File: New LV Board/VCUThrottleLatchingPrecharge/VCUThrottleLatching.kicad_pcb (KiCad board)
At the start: 2 copper layers, 70.3 x 45 mm, 30 parts, among them J1 B12B-PH-K-S:JST_B12B-PH-K-S, Q1 SS8550, U1 IRLML2060TRPBF, U2 IRLML2060TRPBF, U3 IRLML2060TRPBF, U5 IRLML2060TRPBF, U6 IRLML2060TRPBF, U8 PMV160UP, U9 NE555D

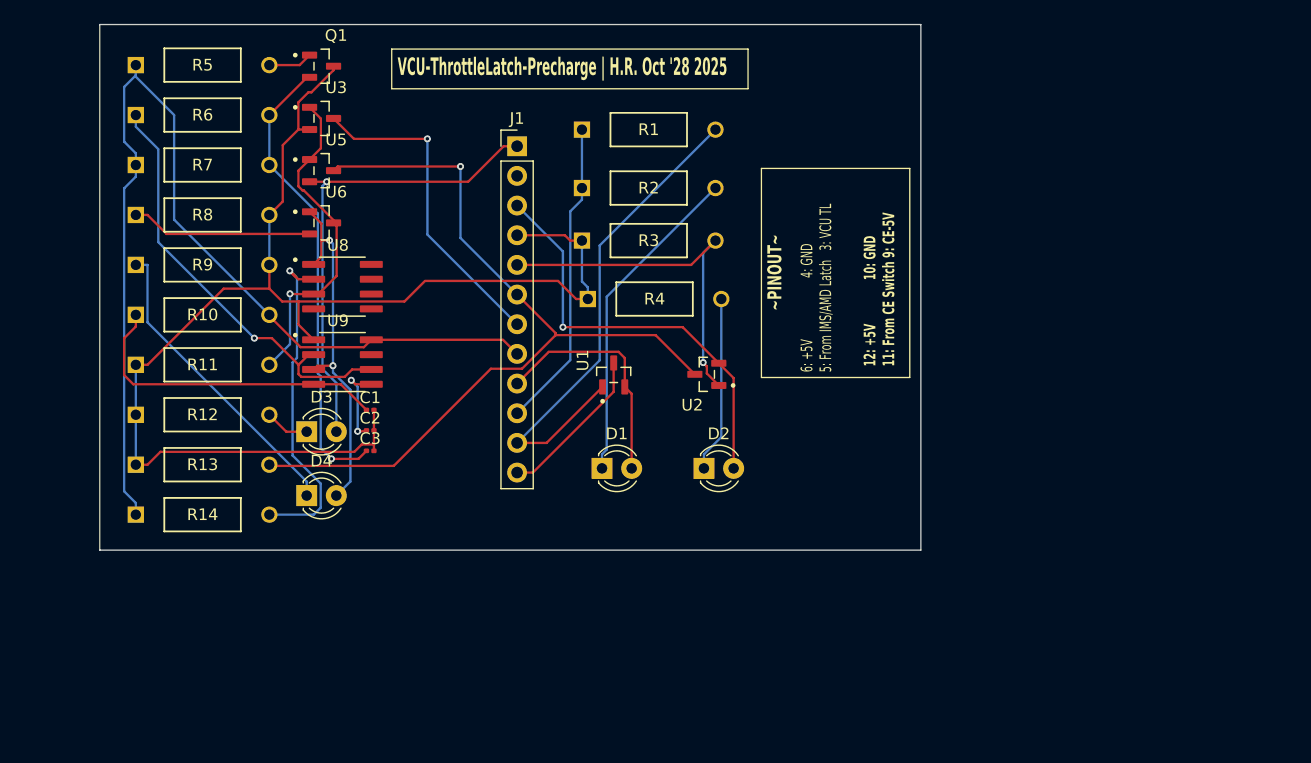
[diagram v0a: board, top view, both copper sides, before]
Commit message: Precharge module added along with file name change
Precharge module added along with file name change
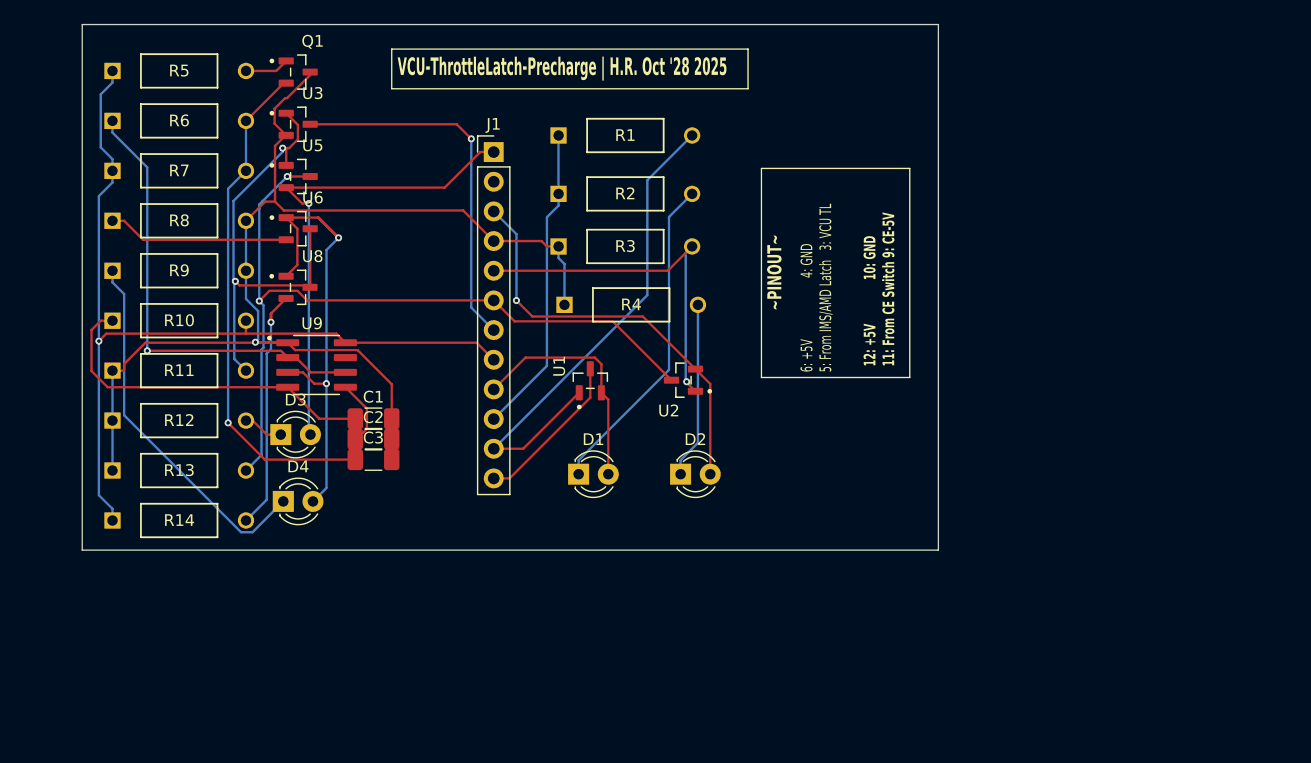
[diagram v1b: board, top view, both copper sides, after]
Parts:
- C1, C2, C3: footprint Capacitor_SMD:C_0201_0603Metric -> Capacitor_SMD:C_1206_3216Metric_Pad1.33x1.80mm_HandSolder
- U8: footprint Footprints:SOIC127P599X175-8N -> Footprints:SOT95P237X112-3N
- moved U8 3.81 mm to (99.5, 93.5)
- moved D3 2.23 mm to (98.0, 106.1)
- moved U9 2.23 mm to (101.1, 100.1)
- moved D1 2.06 mm to (123.5, 109.5)
- moved D2 2.06 mm to (132.2, 109.5)
- moved D4 2.06 mm to (98.2, 111.8)
- moved J1 2.06 mm to (116.2, 81.9)
- moved Q1 2.06 mm to (99.5, 75.1)
- moved R1 2.06 mm to (121.8, 80.5)
- moved R10 2.06 mm to (83.6, 96.4)
- moved R11 2.06 mm to (83.6, 100.6)
- moved R12 2.06 mm to (83.6, 104.9)
- moved R13 2.06 mm to (83.6, 109.2)
- moved R14 2.06 mm to (83.6, 113.5)
- moved R2 2.06 mm to (121.8, 85.5)
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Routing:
- net Net-(D4-A): track 30.8 -> 48.0 mm
- net Net-(U9-VCC): track 88.6 -> 76.4 mm, vias 0 -> 1
- net Net-(Q1-C): track 113.6 -> 103.2 mm, vias 0 -> 1
- net Net-(U3-G): track 28.6 -> 38.6 mm, vias 1 -> 2
- net Net-(R14-Pad2): track 31.7 -> 23.4 mm
- net Net-(D4-K): track 26.4 -> 31.7 mm
- net Net-(Q1-E): track 39.7 -> 43.5 mm
- net Net-(U3-D): track 27.8 -> 31.5 mm
- net Net-(U2-D): track 71.3 -> 67.7 mm, vias 1 -> 2
- net Net-(U9-R): track 27.6 -> 29.9 mm
- net Net-(U9-CV): track 7.61 -> 5.69 mm, vias 2 -> 0
- net Net-(U9-THR): track 37.1 -> 38.7 mm
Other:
- board size 70.3 x 45 mm -> 73.3 x 45 mm

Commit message: got carried away and made a new VCU throttle latching
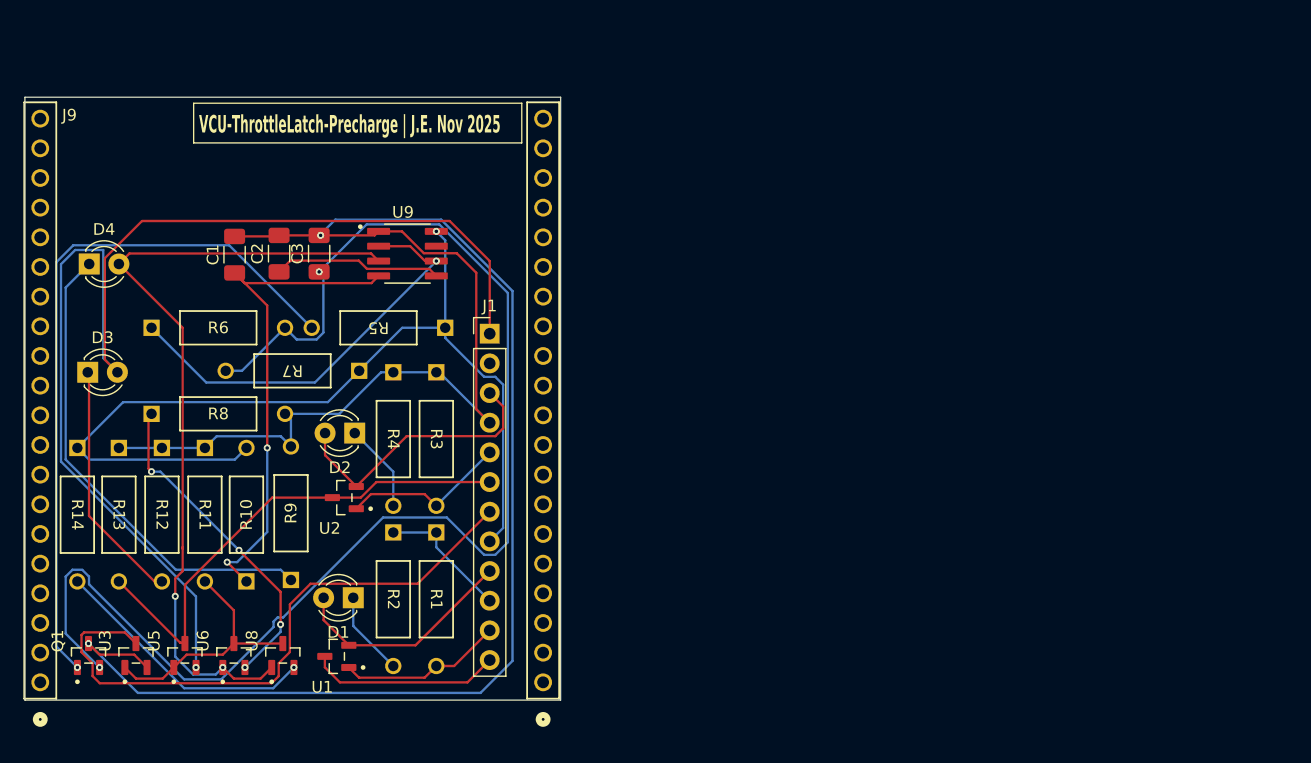
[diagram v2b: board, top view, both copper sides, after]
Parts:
- added J6: PH1-20-UA, PH1-20-UA:CONN_PH1-20-UA_ADM, F.Cu at (120.5, 127.3)
- added J9: PH1-20-UA, PH1-20-UA:CONN_PH1-20-UA_ADM, F.Cu at (77.4, 127.3)
- moved Q1 53.1 mm to (81.5, 125.0), turned to 90 degrees
- moved U3 47.6 mm to (85.6, 125.0), turned to 90 degrees
- moved U5 42.1 mm to (89.8, 125.0), turned to 90 degrees
- moved U6 37.0 mm to (94.0, 125.0), turned to 90 degrees
- moved R5 36.0 mm to (112.1, 97.0), turned to 180 degrees
- moved R1 35.6 mm to (111.3, 114.5), turned to -90 degrees
- moved R2 32.3 mm to (107.6, 114.5), turned to -90 degrees
- moved U1 32.1 mm to (102.8, 125.1), turned to 180 degrees
- moved U8 31.5 mm to (98.2, 125.0), turned to 90 degrees
- moved U2 30.7 mm to (103.4, 111.5)
- moved R9 30.6 mm to (98.9, 118.6), turned to 90 degrees
- moved D2 28.1 mm to (104.3, 106.0), turned to 180 degrees
- moved R7 27.2 mm to (104.7, 100.6), turned to 180 degrees
- moved D4 26.3 mm to (81.6, 91.5)
- moved R10 25.1 mm to (95.1, 118.7), turned to 90 degrees
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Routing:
- net Net-(Q1-E): track 43.5 -> 116.7 mm, vias 1 -> 2
- net Net-(Q1-C): track 103.2 -> 171.3 mm, vias 1 -> 2
- net Net-(D3-A): track 41.4 -> 106.5 mm
- net Net-(Q1-B): track 3.80 -> 60.8 mm, vias 0 -> 1
- net Net-(U1-G): track 43.2 -> 14.1 mm
- net Net-(U2-D): track 67.7 -> 42.6 mm, vias 2 -> 0
- net Net-(D4-A): track 48.0 -> 69.1 mm
- net Net-(U3-D): track 31.5 -> 52.4 mm, vias 1 -> 0
- net Net-(D1-K): track 28.0 -> 7.26 mm
- net Net-(D3-K): track 3.48 -> 20.9 mm
- net Net-(U3-G): track 38.6 -> 21.5 mm, vias 2 -> 0
- net Net-(U2-G): track 30.8 -> 14.2 mm, vias 1 -> 0
- net Net-(J1-Pad10): track 26.6 -> 11.4 mm
- net Net-(U9-R): track 29.9 -> 43.1 mm, vias 0 -> 2
- net Net-(U6-S): track 15.6 -> 28.2 mm, vias 0 -> 4
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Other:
- board size 73.3 x 45 mm -> 45.9 x 51.6 mm
- board text added: "VCU-ThrottleLatch-Precharge | J.E. Nov 2025"
- board text removed: "12: +5V 10: GND 11: From CE Switch 9: CE-5V"
- board text removed: "6: +5V 4: GND 5: From IMS/AMD Latch 3: VCU TL"
- board text removed: "VCU-ThrottleLatch-Precharge | H.R. Oct '28 2025"
- board text removed: "~PINOUT~"

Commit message: VCU Throttle Latching
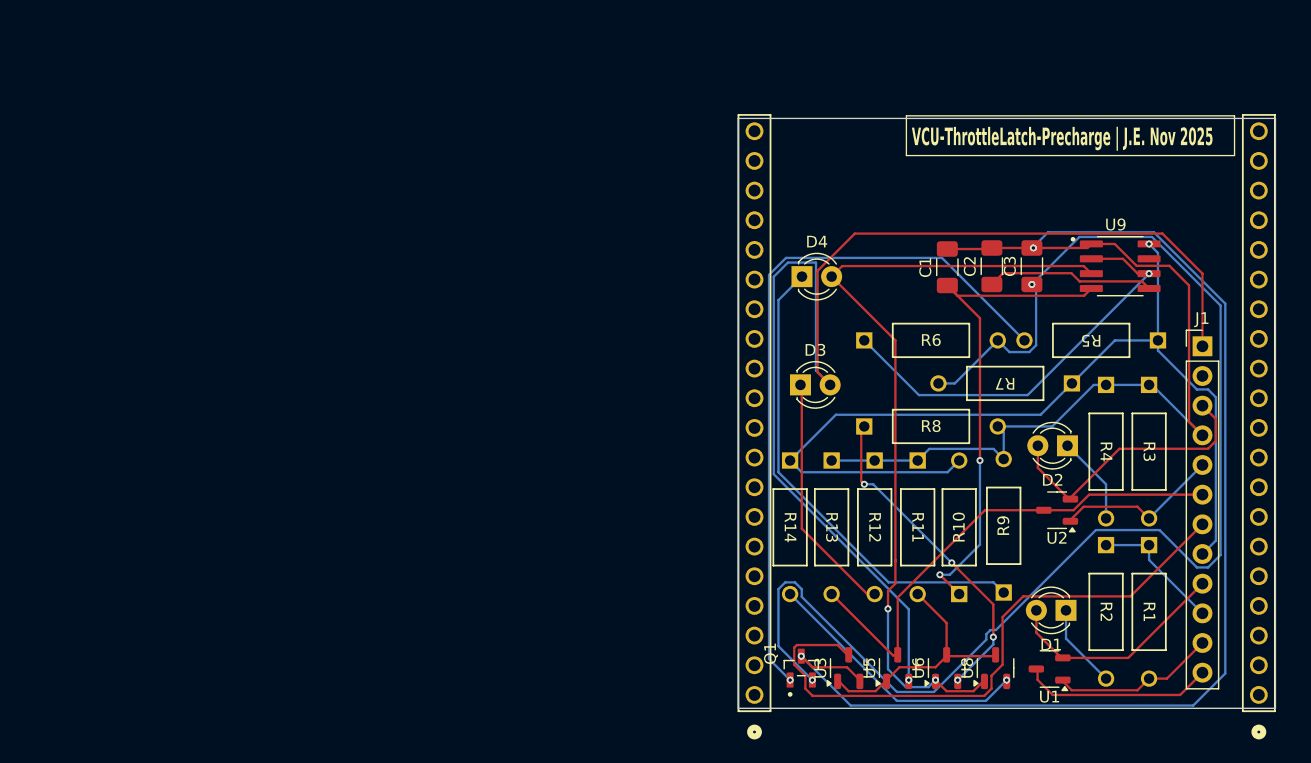
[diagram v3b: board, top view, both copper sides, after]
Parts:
- U1, U2, U3, U5, U6, U8: footprint Footprints:SOT95P237X112-3N -> Package_TO_SOT_SMD:SOT-23-3
- moved P2 61.3 mm to (181.7, 128.4)
- moved P1 61.2 mm to (138.6, 128.4)
- moved C1 61.0 mm to (155.1, 91.8)
- moved C2 61.0 mm to (158.9, 91.7)
- moved C3 61.0 mm to (162.3, 91.7)
- moved D2 61.0 mm to (165.4, 107.1)
- moved D4 61.0 mm to (142.6, 92.6)
- moved R2 61.0 mm to (168.7, 115.6)
- moved R4 61.0 mm to (168.7, 101.9)
- moved R6 61.0 mm to (148.0, 98.0)
- moved R7 61.0 mm to (165.7, 101.7)
- moved R8 61.0 mm to (148.0, 105.4)
- moved D1 61.0 mm to (165.2, 121.2)
- moved D3 61.0 mm to (142.5, 101.9)
- moved J1 61.0 mm to (176.9, 98.6)
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- renumbered J9 to P1, J6 to P2
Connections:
- J1 pad 10: Net-(J1-Pad10) -> Net-(Q1-C)
- J1 pad 6: Net-(U2-D) -> Net-(U1-D)
- R1 pad 1: Net-(J1-Pad10) -> Net-(Q1-C)
- R13 pad 2: Net-(U2-D) -> Net-(U1-D)
- R2 pad 1: Net-(J1-Pad10) -> Net-(Q1-C)
- U2 pad 3: Net-(U2-D) -> Net-(U1-D)
- U5 pad 3: Net-(U2-D) -> Net-(U1-D)
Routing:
- net Net-(U2-D): track 42.6 -> 0.00 mm
- net Net-(U1-D): track 16.4 -> 59.0 mm
- net Net-(J1-Pad10): track 11.4 -> 0.00 mm
- net Net-(Q1-C): track 171.3 -> 182.8 mm
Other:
- board size 45.9 x 51.6 mm -> 46 x 50.5 mm
